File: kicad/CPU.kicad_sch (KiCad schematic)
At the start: 49 parts, among them SW1 SW_Push, U11 STM32F303CBTx, U7 MC34063AD, U8 MC34063AD, U9 LD1117S33TR_SOT223, X1 8 MHz

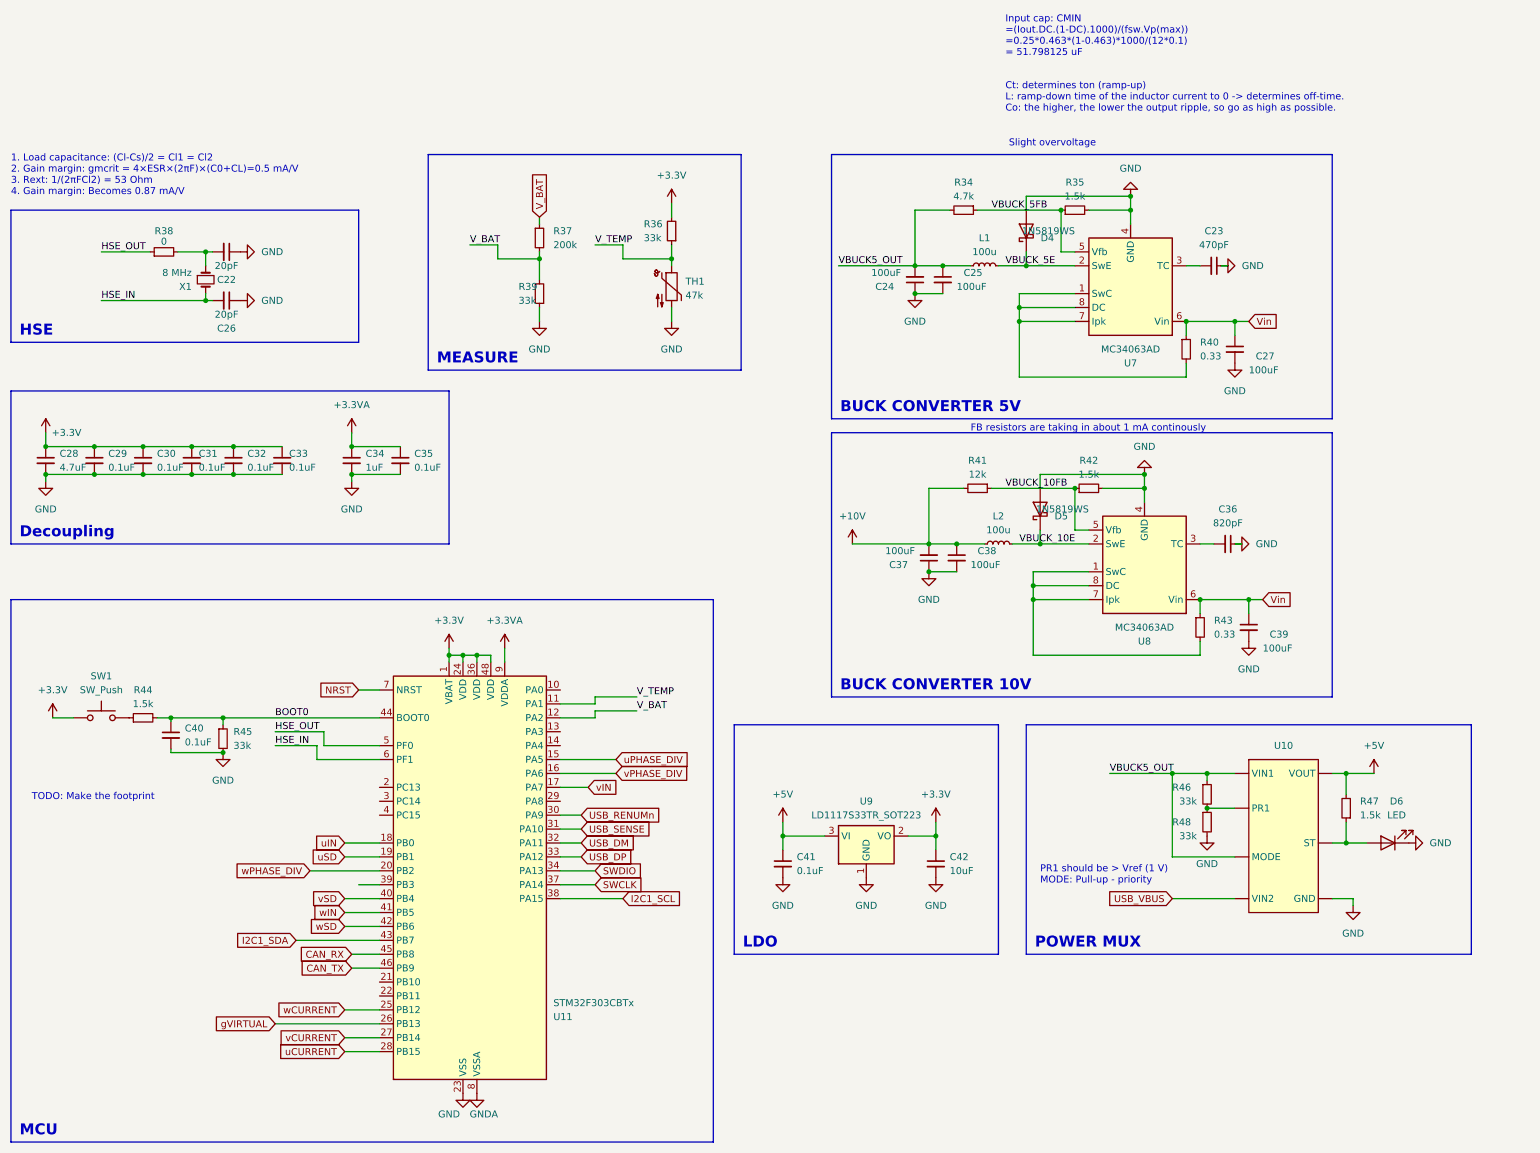
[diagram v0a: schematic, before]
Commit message: [kicad] added soldering pads for phases and battery connectors, rearranged schematic, added tooling holes, fixed ERC errors [scripts] minor footprint calculations
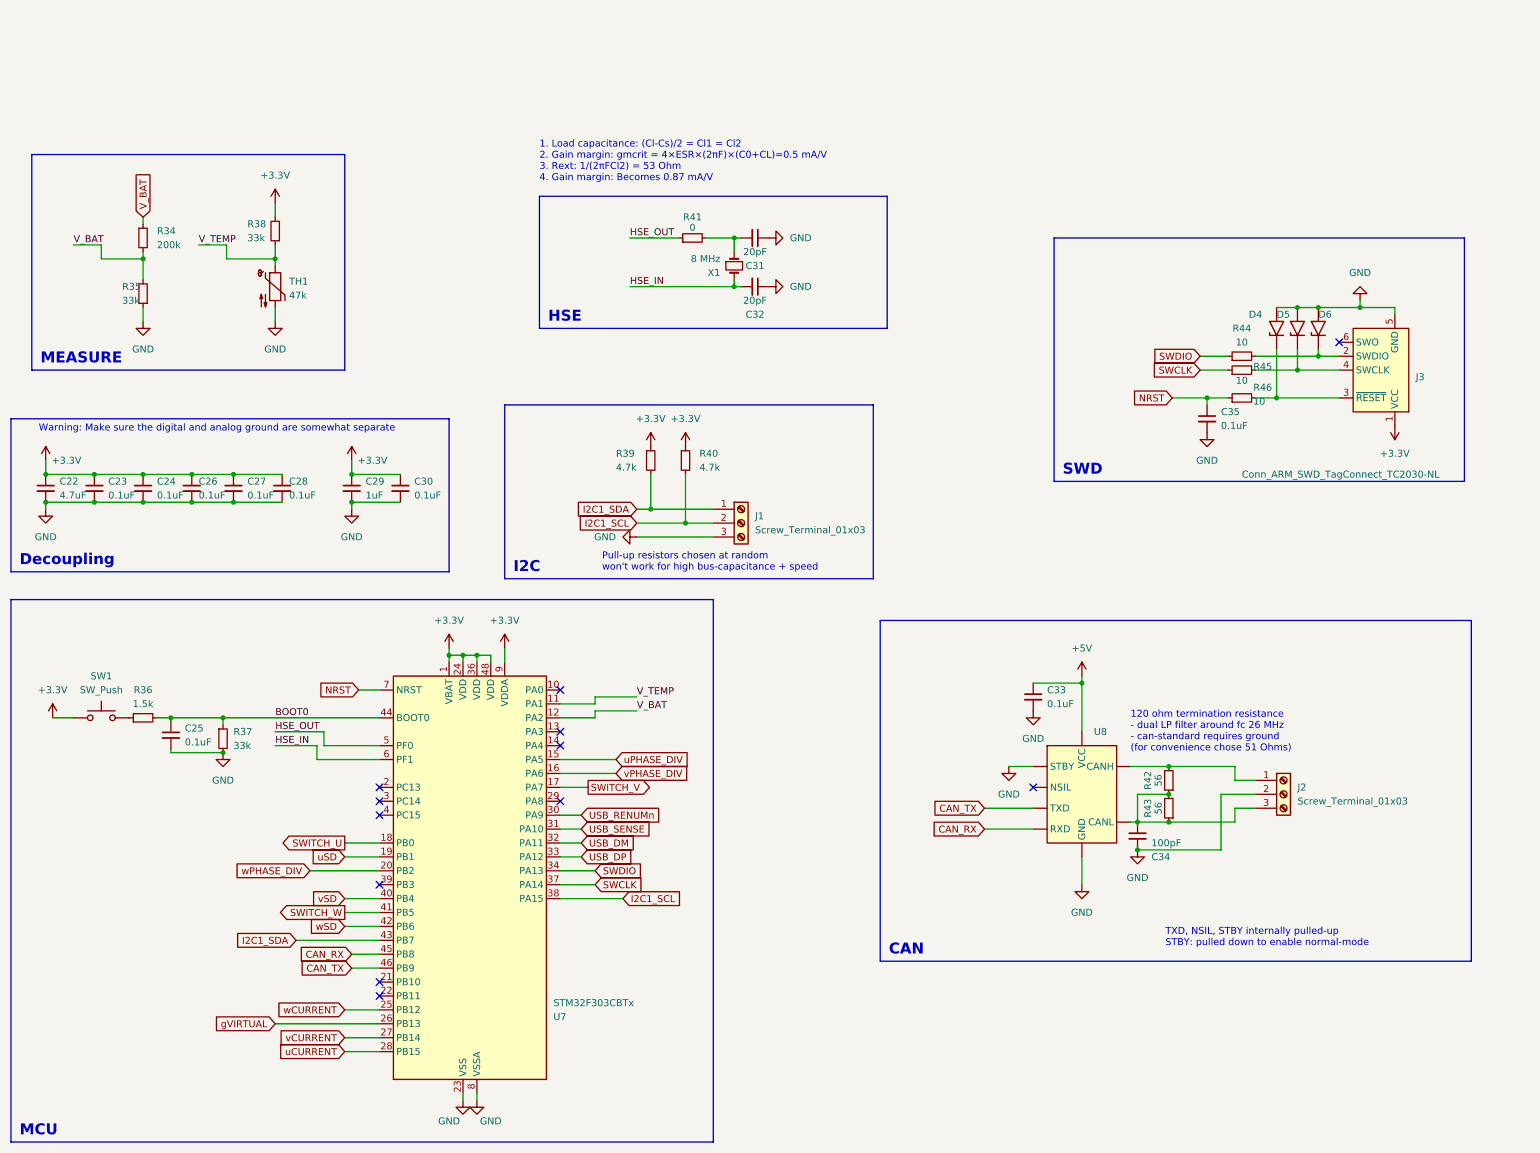
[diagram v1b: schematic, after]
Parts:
- removed C23: 470pF, Capacitor_SMD:C_0805_2012Metric, symbol Device:C_Small
- removed C24, C25, C27, C37, C38, C39: 100uF, Capacitor_SMD:C_1210_3225Metric, symbol Device:C_Small
- removed C36: 820pF, Capacitor_SMD:C_0805_2012Metric, symbol Device:C_Small
- removed C41: 0.1uF, Resistor_SMD:R_0402_1005Metric, symbol Device:C_Small
- removed C42: 10uF, Capacitor_SMD:C_0402_1005Metric, symbol Device:C_Small
- removed D4, D5: 1N5819WS, Diode_SMD:D_SOD-323, symbol Diode:1N5819
- removed D6: LED, LED_SMD:LED_0805_2012Metric, symbol Device:LED
- removed L1, L2: 100u, Inductor_SMD:L_1210_3225Metric, symbol Device:L_Small
- removed R34: 4.7k, Resistor_SMD:R_0805_2012Metric, symbol Device:R_Small
- removed R35, R47: 1.5k, Resistor_SMD:R_0805_2012Metric, symbol Device:R_Small
- removed R41: 12k, Resistor_SMD:R_0603_1608Metric, symbol Device:R_Small
- removed R48: 33k, Resistor_SMD:R_0603_1608Metric, symbol Device:R_Small
- removed U10: ~, Package_TO_SOT_SMD:SOT-583-8, symbol bldc:TPS2116
- removed U7, U8: MC34063AD, Package_SO:SOIC-8_3.9x4.9mm_P1.27mm, symbol Regulator_Switching:MC34063AD
- removed U9: LD1117S33TR_SOT223, Package_TO_SOT_SMD:SOT-223-3_TabPin2, symbol Regulator_Linear:LD1117S33TR_SOT223
- added C33, C35: 0.1uF, Resistor_SMD:R_0402_1005Metric, symbol Device:C_Small
- added C34: 100pF, Capacitor_SMD:C_0603_1608Metric, symbol Device:C_Small
- added D4, D5, D6: SMAJ6.5CA, Diode_SMD:D_SMA, symbol Diode:SMAJ13A
- added J1: Screw_Terminal_01x03, TerminalBlock:TerminalBlock_bornier-3_P5.08mm, symbol Connector:Screw_Terminal_01x03
- added J2: Screw_Terminal_01x03, bldc:Ningbo-Kangnex-Elec_3x1-WJ500V-5.08-3P, symbol Connector:Screw_Terminal_01x03
- added J3: Conn_ARM_SWD_TagConnect_TC2030-NL, Connector:Tag-Connect_TC2030-IDC-NL_2x03_P1.27mm_Vertical, symbol Connector:Conn_ARM_SWD_TagConnect_TC2030-NL
- added R39: 4.7k, Resistor_SMD:R_0805_2012Metric, symbol Device:R_Small
- added R44, R45: 10, Resistor_SMD:R_1206_3216Metric, symbol Device:R_Small
- added U8: ~, bldc:MICROCHIP_CAN_ATA6560-GAQW-N, symbol bldc:ATA6560
- R40: value 0.33 -> 4.7k; footprint Resistor_SMD:R_2512_6332Metric -> Resistor_SMD:R_0805_2012Metric; MFR.Part 25121WF330LT4E -> 0805W8F4701T5E; jlcpcb C25468 -> C17673
- R42: value 1.5k -> 56; footprint Resistor_SMD:R_0805_2012Metric -> Resistor_SMD:R_0603_1608Metric; MFR.Part (none) -> 0603WAD560JT5E; jlcpcb C4310 -> C423025
- R43: value 0.33 -> 56; footprint Resistor_SMD:R_2512_6332Metric -> Resistor_SMD:R_0603_1608Metric; MFR.Part 25121WF330LT4E -> 0603WAD560JT5E; jlcpcb C25468 -> C423025
- R46: value 33k -> 10; footprint Resistor_SMD:R_0603_1608Metric -> Resistor_SMD:R_1206_3216Metric; MFR.Part (none) -> 1206W4F100JT5E; jlcpcb C4216 -> C17903
- SW1: footprint (none) -> bldc:ALPSALPINE_BUTTON_SPEH110100
- renumbered C28 to C22, C29 to C23, C30 to C24, C40 to C25, C31 to C26, C32 to C27, C33 to C28, C34 to C29, C35 to C30, C22 to C31, C26 to C32, R37 to R34, R39 to R35, R44 to R36, R45 to R37, R36 to R38, R38 to R41, U11 to U7
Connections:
- net +3.3VA is gone; now on net +3.3V: C29.1, C30.1, U7.9 (VDDA)
- net GNDA is gone; now on net GND: U7.8 (VSSA)
- net VBUCK5_OUT is gone; now on net NRST: R46.1
- net VBUCK_10FB is gone; now on an unnamed net: R42.1
- net +3.3V: now also R40.1, J3.1 (VCC), R39.1
- net +5V: now also C33.1, U8. (VCC)
- net CAN_RX: now also U8. (VCC)
- net CAN_TX: now also U8. (VCC)
- net GND: now also C33.2, C34.2, C35.2, D4.2 (A2), D5.2 (A2), D6.2 (A2), J1.3 (Pin_3), J2.2 (Pin_2), J3.5 (GND), U8. (VCC); no longer R42.2
- net I2C1_SCL: now also R40.2, J1.2 (Pin_2)
- net I2C1_SDA: now also J1.1 (Pin_1), R39.2
- net NRST: now also C35.1
- net SWCLK: now also R45.1
- net SWDIO: now also R44.1
- net at R46.2: now also D4.1 (A1), J3.3 (~{RESET})
- net at R43.2: now also R43.1, C34.1, J2.3 (Pin_3), U8. (VCC)
- removed net Vin: R40.1, R43.1
- net uIN renamed SWITCH_U
- net vIN renamed SWITCH_V
- net wIN renamed SWITCH_W
- new net: J2.1 (Pin_1), R42.2, U8. (VCC)
- new net: D6.1 (A1), J3.2 (SWDIO), R44.2
- new net: D5.1 (A1), J3.4 (SWCLK), R45.2
- no-connect marks 0 -> 12
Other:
- note added: "120 ohm termination resistance - dual LP filter around fc 26 MHz - can-standard requires ground (for convenience chose 51 Ohms)"
- note added: "Pull-up resistors chosen at random won't work for high bus-capacitance + speed"
- note added: "TXD, NSIL, STBY internally pulled-up STBY: pulled down to enable normal-mode"
- note added: "Warning: Make sure the digital and analog ground are somewhat separate"
- note removed: "Ct: determines ton (ramp-up) L: ramp-down time of the inductor current to 0 -> determines off-time. Co: the higher, the lower the output ripple, so go as high as possible."
- note removed: "FB resistors are taking in about 1 mA continously"
- note removed: "Input cap: CMIN =(Iout.DC.(1-DC).1000)/(fsw.Vp(max)) =0.25*0.463*(1-0.463)*1000/(12*0.1) = 51.798125 uF"
- note removed: "PR1 should be > Vref (1 V) MODE: Pull-up - priority"
- note removed: "Slight overvoltage"
- note removed: "TODO: Make the footprint"
- company: (none) -> Igor Wolfs
- title: (none) -> BLDC Driver Project
- moved on the sheet: C22, C23, C24, C26, C27, C28, C29, C30, C31, C32, R34, R35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

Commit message: [bldc] Fixed footprint issues, added jlcpcb man. rules, stackup decisions, added nets..
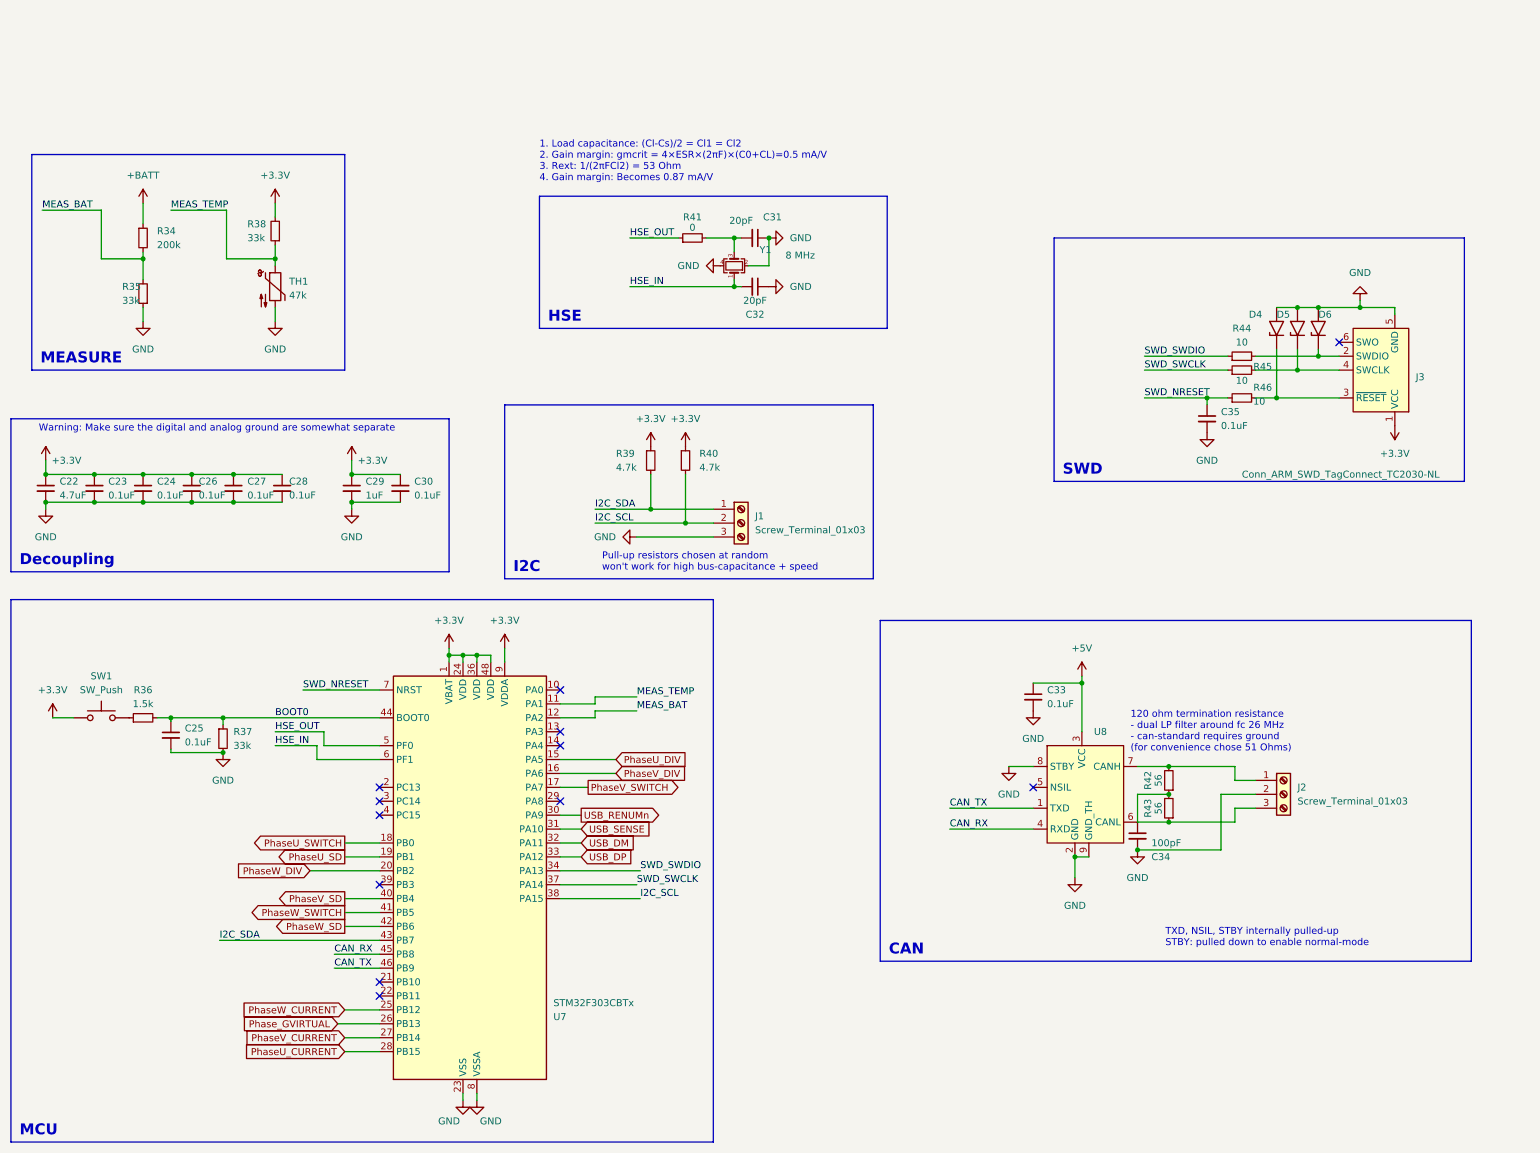
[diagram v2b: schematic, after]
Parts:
- removed X1: 8 MHz, Crystal:Crystal_SMD_3225-4Pin_3.2x2.5mm, symbol Device:Crystal_Small
- added Y1: 8 MHz, Crystal:Crystal_SMD_3225-4Pin_3.2x2.5mm, symbol Device:Crystal_GND24_Small
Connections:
- net +5V: now also U8.3 (VCC); no longer U8. (VCC)
- net CAN_RX: now also U8.4 (RXD); no longer U8. (VCC)
- net CAN_TX: now also U8.1 (TXD); no longer U8. (VCC)
- net GND: now also U8.2 (GND), U8.8 (STBY), U8.9 (GND_TH), Y1.2, Y1.4; no longer U8. (VCC)
- net HSE_IN: now also Y1.1
- net at C31.2, R41.2: now also Y1.3
- net at C34.1, J2.3 (Pin_3), R42.1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: now also U8.6 (CANL); no longer U8. (VCC)
- net at J2.1 (Pin_1), R42.2: now also U8.7 (CANH); no longer U8. (VCC)
- net I2C1_SCL renamed I2C_SCL
- net I2C1_SDA renamed I2C_SDA
- net NRST renamed SWD_NRESET
- net SWCLK renamed SWD_SWCLK
- net SWDIO renamed SWD_SWDIO
- net SWITCH_U renamed PhaseU_SWITCH
- net SWITCH_V renamed PhaseV_SWITCH
- net SWITCH_W renamed PhaseW_SWITCH
- net V_BAT renamed MEAS_BAT
- net MEAS_BAT: no longer R34.1
- net V_TEMP renamed MEAS_TEMP
- net gVIRTUAL renamed Phase_GVIRTUAL
- net uCURRENT renamed PhaseU_CURRENT
- net uPHASE_DIV renamed PhaseU_DIV
- net uSD renamed PhaseU_SD
- net vCURRENT renamed PhaseV_CURRENT
- net vPHASE_DIV renamed PhaseV_DIV
- net vSD renamed PhaseV_SD
- net wCURRENT renamed PhaseW_CURRENT
- net wPHASE_DIV renamed PhaseW_DIV
- net wSD renamed PhaseW_SD
- new net +BATT: R34.1

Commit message: [kicad] basic placement of everything but power and inverter, changed the ldo, changed caps
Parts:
- added C31: 1uF, Capacitor_SMD:C_1206_3216Metric, symbol Device:C_Small
- added FB1: 120R, Resistor_SMD:R_0603_1608Metric, symbol Device:FerriteBead_Small
- renumbered C35 to C32, C31 to C35, C32 to C36, J3 to J1, J1 to J3, R44 to R39, R45 to R40, R46 to R41, R39 to R44, R41 to R45, R40 to R46
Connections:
- net +3.3V: now also C31.1, FB1.2; no longer C29.1, C30.1, U7.9 (VDDA)
- net GND: now also J2.1 (Pin_1), J3.1 (Pin_1), C31.2; no longer J2.2 (Pin_2), J3.3 (Pin_3)
- net I2C_SCL: now also J3.3 (Pin_3), R44.2; no longer J3.2 (Pin_2), R46.2
- net I2C_SDA: now also J3.2 (Pin_2), R46.2; no longer J3.1 (Pin_1), R44.2
- net at C34.1, R42.1, R43.1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: now also J2.2 (Pin_2); no longer J2.3 (Pin_3)
- net at R42.2, U8.7 (CANH): now also J2.3 (Pin_3); no longer J2.1 (Pin_1)
- new net +3.3VA: C29.1, C30.1, FB1.1, U7.9 (VDDA)
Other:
- moved on the sheet: C32, C35, C36, D4, D5, D6, J1, J3, R39, R40, R41, R44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
